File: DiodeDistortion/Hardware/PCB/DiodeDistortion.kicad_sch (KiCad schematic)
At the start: 21 parts, among them J1 THONKICONN, J2 THONKICONN, J3 THONKICONN, J4 Conn_01x10_Pin, U1 TL074, U3 NSL-32

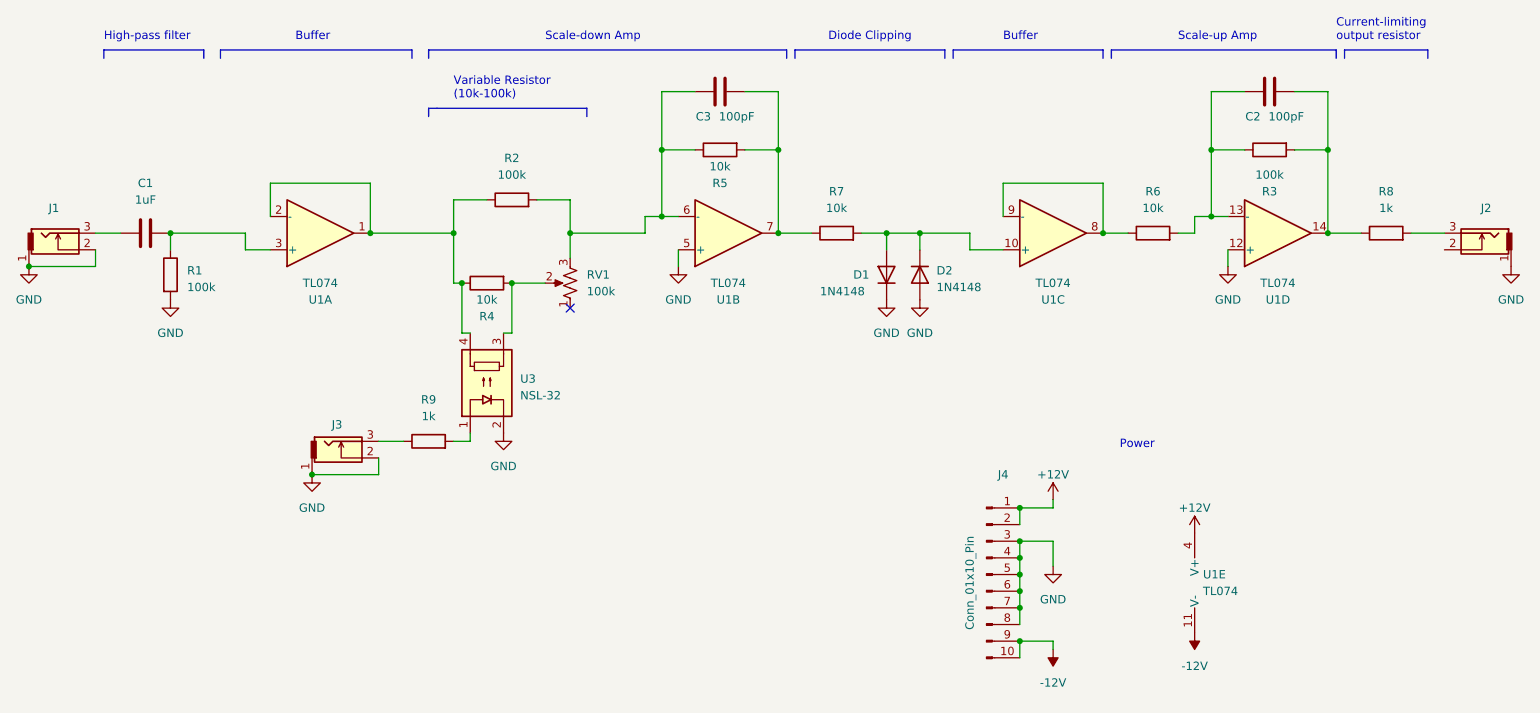
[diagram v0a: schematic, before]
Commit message: Added power filtering to diode distortion
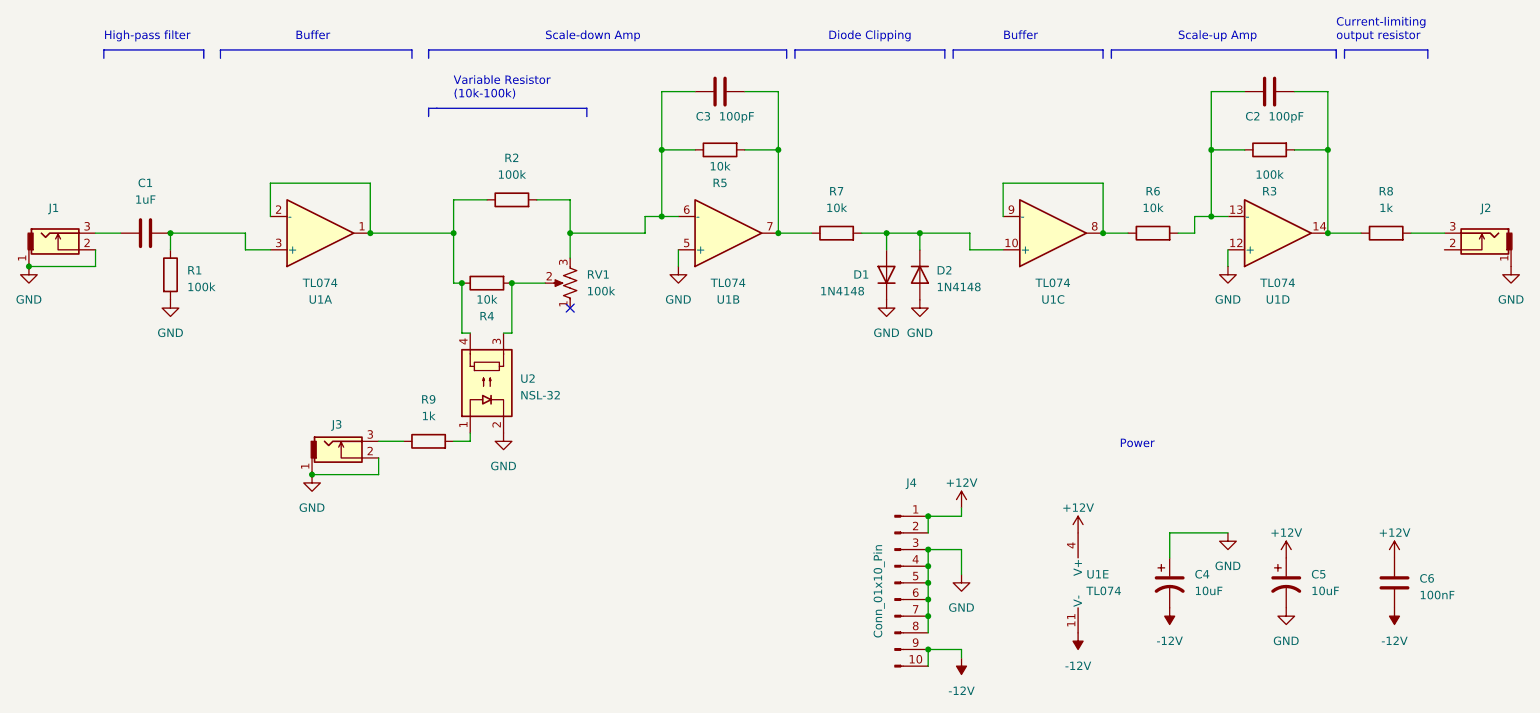
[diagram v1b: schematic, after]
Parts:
- added C4, C5: 10uF, Capacitor_THT:CP_Radial_D4.0mm_P2.00mm, symbol Device:C_Polarized_US
- added C6: 100nF, Capacitor_THT:C_Disc_D4.7mm_W2.5mm_P5.00mm, symbol Device:C
- renumbered U3 to U2
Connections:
- net +12V: now also C5.1, C6.1
- net -12V: now also C4.2, C6.2
- net GND: now also C4.1, C5.2
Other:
- moved on the sheet: J4, U1E
